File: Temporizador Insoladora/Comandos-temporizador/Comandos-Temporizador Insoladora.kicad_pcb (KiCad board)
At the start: 2 copper layers, 59.7 x 30.5 mm, 5 parts, among them P7 CONN_02X08

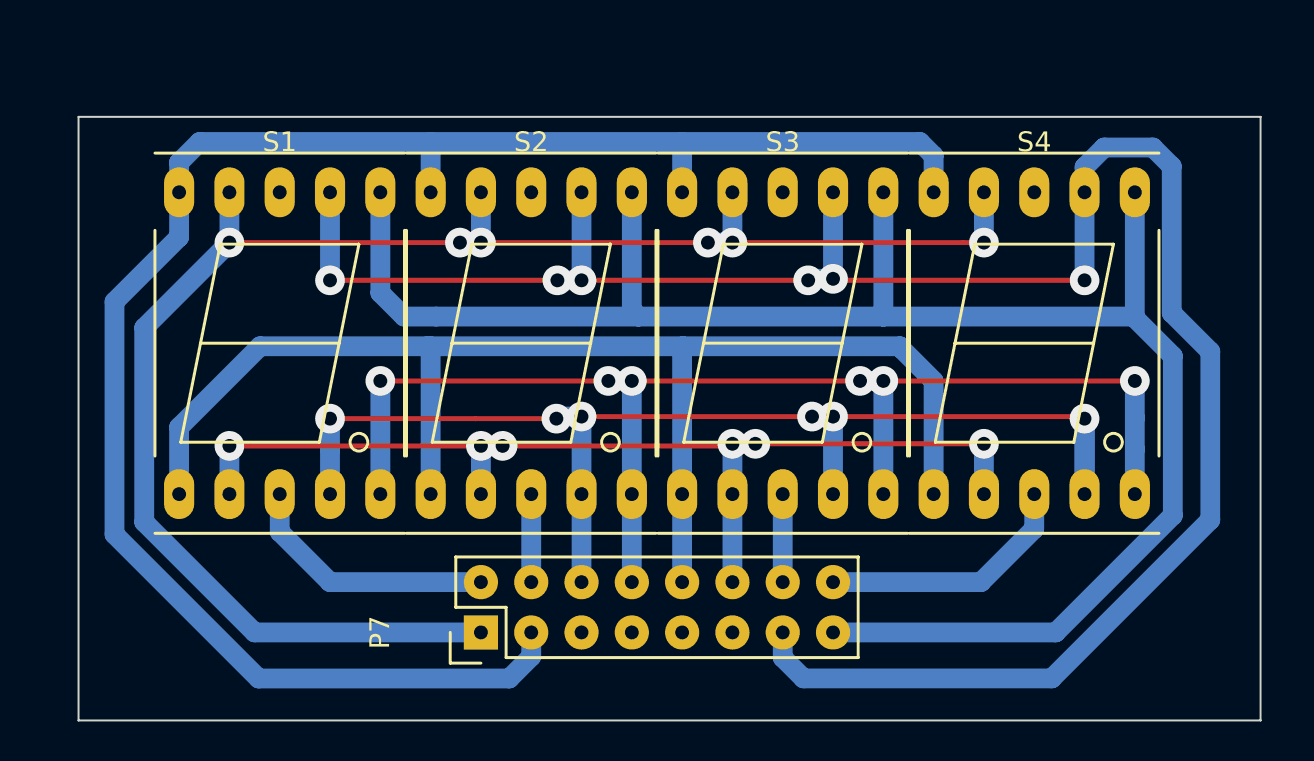
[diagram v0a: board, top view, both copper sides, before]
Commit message: Cambiado tamaño de footprint del capacitor y varistor de la parte de potencia
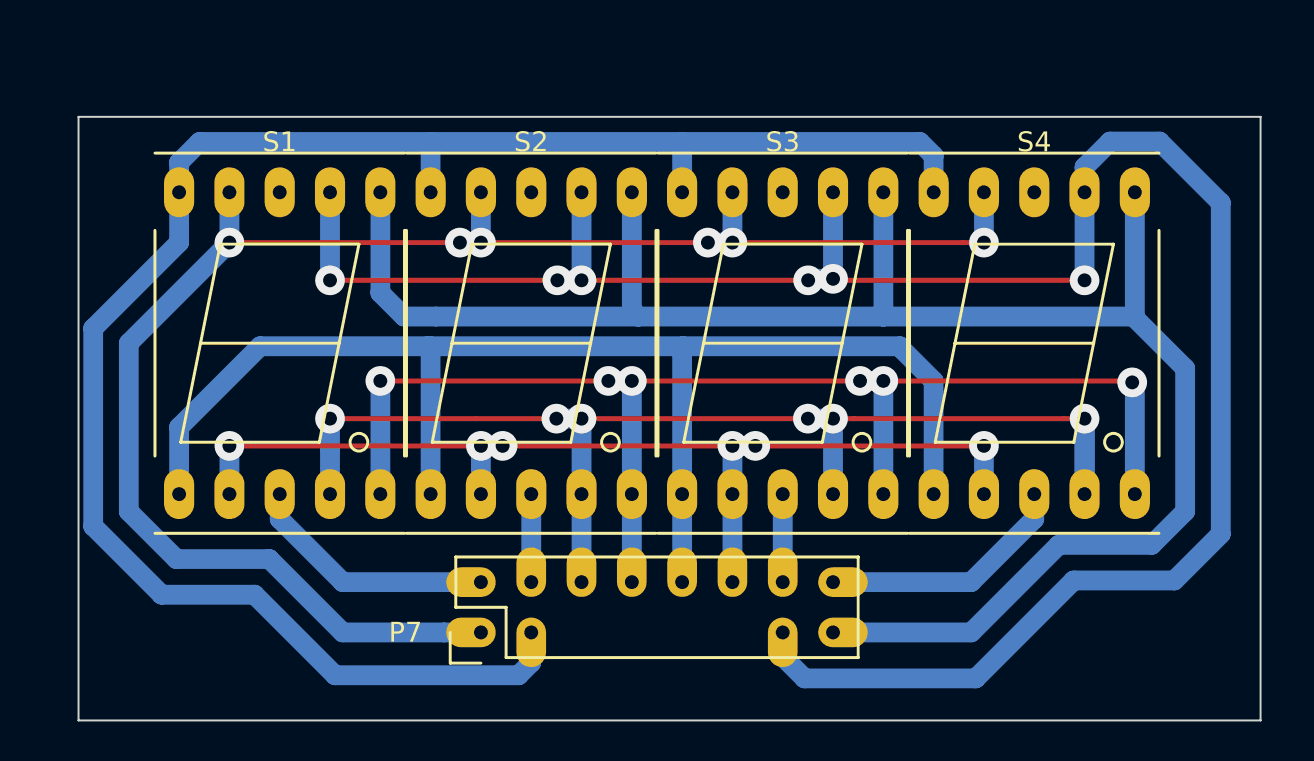
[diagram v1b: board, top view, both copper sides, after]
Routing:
- net /A: track 107.6 -> 109.4 mm
- net /G: track 91.6 -> 92.9 mm
- net /F: track 83.5 -> 84.3 mm
- net /B: track 93.1 -> 93.9 mm
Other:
- net class Default: clearance 0.5 -> 0.6
- rule trace_clearance: 0.5 -> 0.6

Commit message: Acomodando las referencias de los compònentes para el top silk
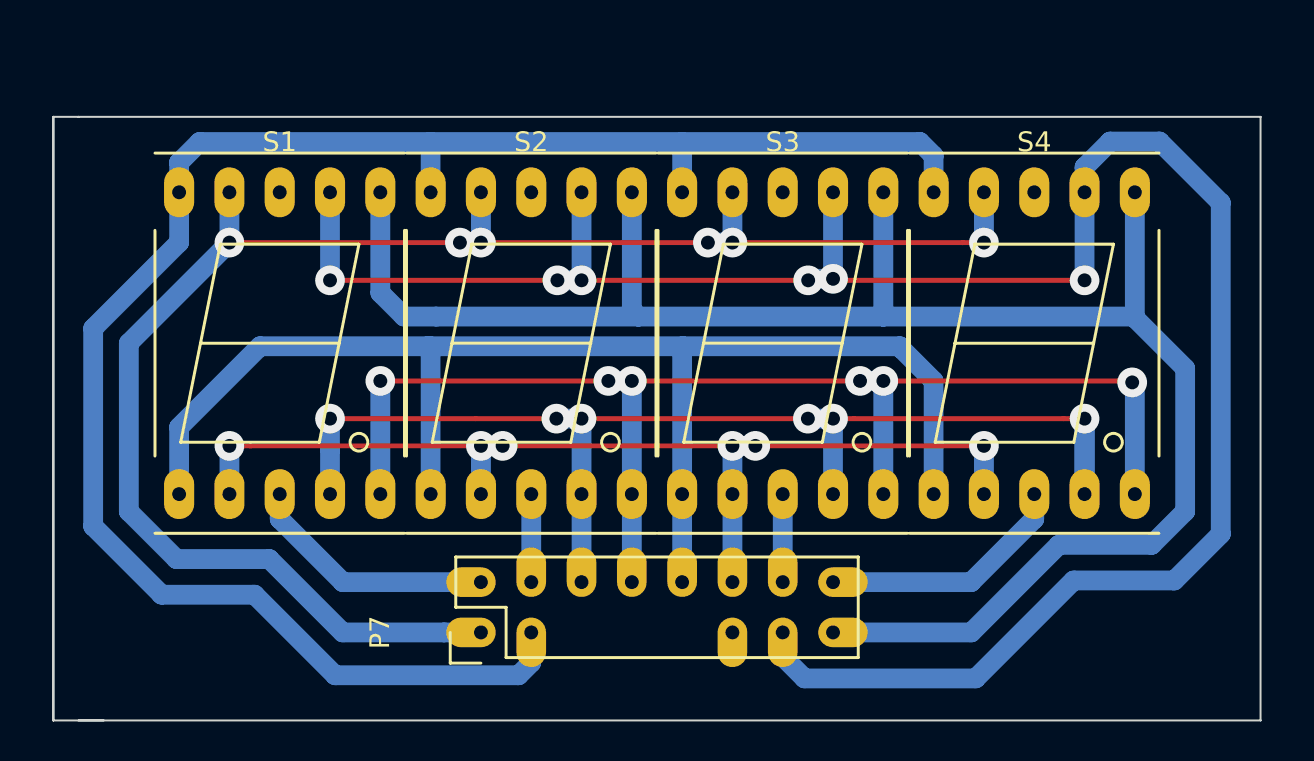
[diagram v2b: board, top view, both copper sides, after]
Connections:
- S1 pad 8: (no net) -> Net-(S1-Pad8)
- S2 pad 8: (no net) -> Net-(S2-Pad8)
- S3 pad 8: (no net) -> Net-(S3-Pad8)
- S4 pad 8: (no net) -> Net-(S4-Pad8)
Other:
- board size 59.7 x 30.5 mm -> 61 x 30.5 mm
- net class Default: clearance 0.6 -> 0.5
- rule trace_clearance: 0.6 -> 0.5

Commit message: Agregado plano de masa al display
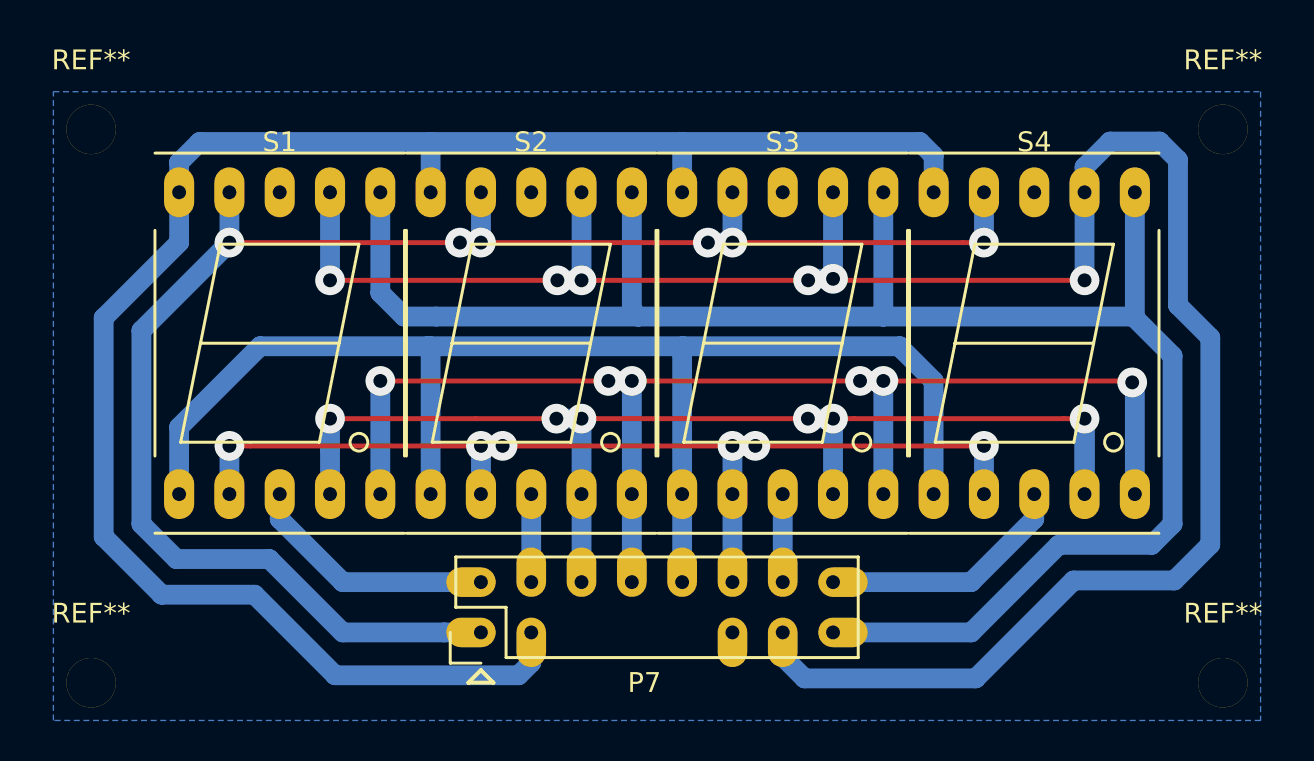
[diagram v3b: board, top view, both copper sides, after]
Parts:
- added REF**: MountingHole_2-5mm, Mounting_Holes:MountingHole_2-5mm, F.Cu at (128.9, 67.9)
- added REF**: MountingHole_2-5mm, Mounting_Holes:MountingHole_2-5mm, F.Cu at (128.9, 40.0)
- added REF**: MountingHole_2-5mm, Mounting_Holes:MountingHole_2-5mm, F.Cu at (71.8, 40.0)
- added REF**: MountingHole_2-5mm, Mounting_Holes:MountingHole_2-5mm, F.Cu at (71.8, 67.9)
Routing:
- net /F: track 84.3 -> 83.7 mm
- net /B: track 93.9 -> 93.3 mm
- added copper zone on B.Cu, net GND
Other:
- board outline removed
